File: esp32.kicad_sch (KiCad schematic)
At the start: 50 parts, among them J4 TC2030-IDC, J5 Conn_01x04, J6 Conn_01x06, J8 USB_C_Receptacle_USB2.0, SW1 SWITCH-SPST, SW2 SWITCH-SPST, U5 SN74AVC4T774, U6 ESP32-S3-WROOM-1, Y1 32.768kHz

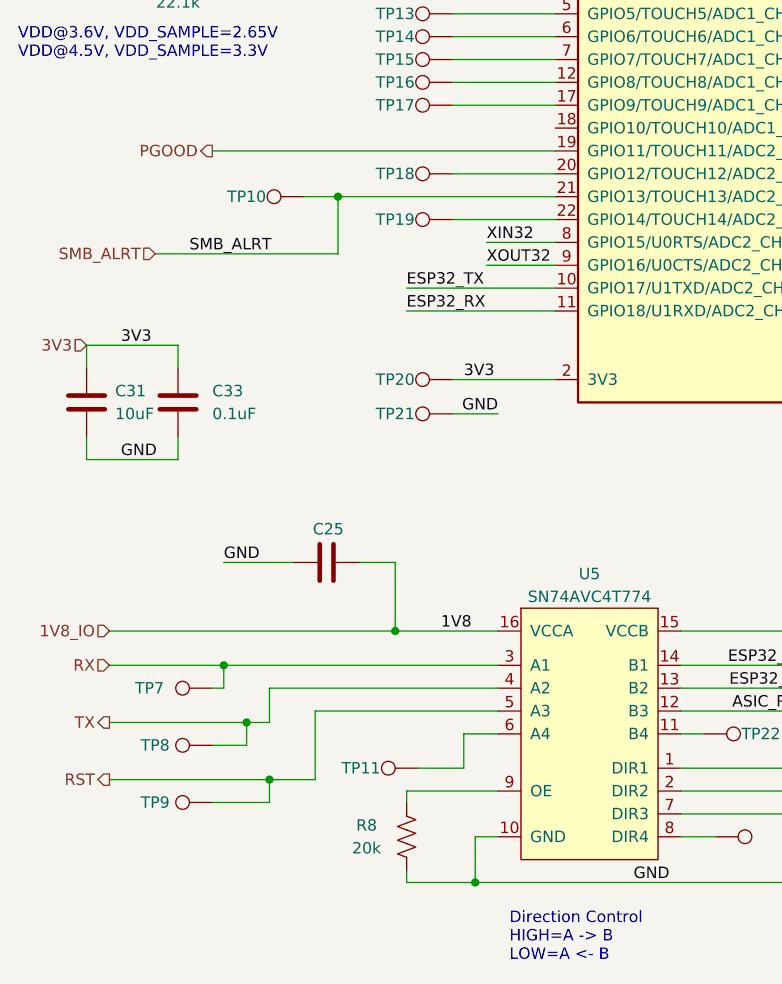
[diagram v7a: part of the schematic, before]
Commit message: add voltage domain sense signals to the ESP32 ADC
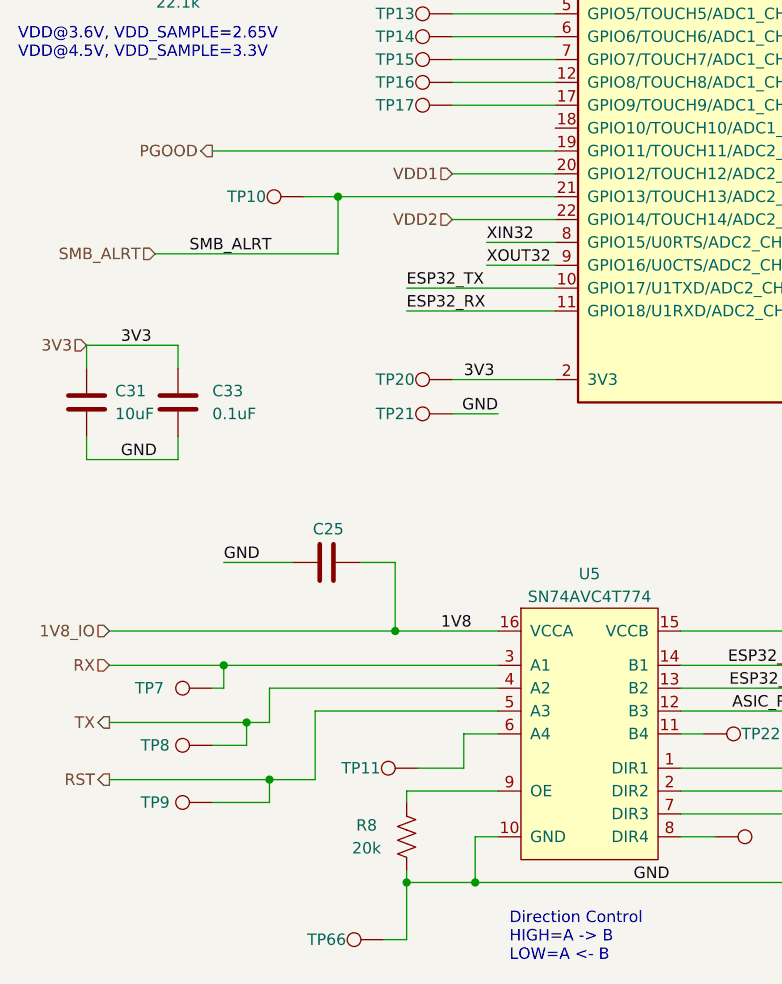
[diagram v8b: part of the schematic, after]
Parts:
- removed TP18, TP19: TestPoint, TestPoint:TestPoint_Pad_D1.0mm, symbol Connector:TestPoint
- added TP66: TestPoint, TestPoint:TestPoint_Pad_D1.0mm, symbol Connector:TestPoint
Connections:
- net GND: now also TP66.1
- net VDD1: now reaches U6.20 (GPIO12/TOUCH12/ADC2_CH1/FSPICLK/FSPIIO6/SUBSPICLK)
- net VDD2: now reaches U6.22 (GPIO14/TOUCH14/ADC2_CH3/FSPIWP/FSPIDQS/SUBSPIWP)
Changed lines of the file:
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@@
 	)
 	(junction
+		(at 57.15 185.42)
+		(diameter 0)
+		(color 0 0 0 0)
+	)
+	(junction
 		(at 36.83 161.29)
 		(diameter 0)
@@
 	(wire
 		(pts
+			(xy 57.15 191.77) (xy 57.15 185.42)
+		)
+		(stroke
+			(width 0)
+			(type default)
+		)
+	)
+	(wire
+		(pts
 			(xy 39.37 49.53) (xy 46.99 49.53)
 		)
@@
 	(wire
 		(pts
+			(xy 54.61 191.77) (xy 57.15 191.77)
+		)
+		(stroke
+			(width 0)
+			(type default)
+		)
+	)
+	(wire
+		(pts
 			(xy 21.59 125.73) (xy 21.59 128.27)
 		)
@@
 		)
 	)
+	(hierarchical_label "VDD2"
+		(shape input)
+		(at 62.23 111.76 180)
+		(fields_autoplaced yes)
+		(effects
+			(font
+				(size 1.27 1.27)
+			)
+			(justify right)
+		)
+	)
 	(hierarchical_label "SCL"
 		(shape input)
@@
 		)
 	)
+	(hierarchical_label "VDD1"
+		(shape input)
+		(at 62.23 106.68 180)
+		(fields_autoplaced yes)
+		(effects
+			(font
+				(size 1.27 1.27)
+			)
+			(justify right)
+		)
+	)
 	(hierarchical_label "SDA"
 		(shape input)
@@
 	(symbol
 		(lib_id "Connector:TestPoint")
+		(at 54.61 191.77 90)
+		(mirror x)
+		(unit 1)
+		(exclude_from_sim no)
+		(in_bom no)
+		(on_board yes)
+		(dnp no)
+		(property "Reference" "TP66"
+			(at 48.26 191.77 90)
+			(effects
+				(font
+					(size 1.27 1.27)
+				)
+			)
+		)
+		(property "Value" "TestPoint"
+			(at 48.895 193.0399 90)
+			(effects
+				(font
+					(size 1.27 1.27)
+				)
+				(justify left)
+				(hide yes)
+			)
+		)
+		(property "Footprint" "TestPoint:TestPoint_Pad_D1.0mm"
+			(at 54.61 196.85 0)
+			(effects
+				(font
+					(size 1.27 1.27)
+				)
+				(hide yes)
+			)
+		)
+		(property "Datasheet" "~"
+			(at 54.61 196.85 0)
+			(effects
+				(font
+					(size 1.27 1.27)
+				)
+				(hide yes)
+			)
+		)
+		(property "Description" ""
+			(at 54.61 191.77 0)
+			(effects
+				(font
+					(size 1.27 1.27)
+				)
+				(hide yes)
+			)
+		)
+		(pin "1"
+		)
+		(instances
+			(project "bitaxeHex"
+				(path "/e63e39d7-6ac0-4ffd-8aa3-1841a4541b55/ca857324-2ec8-447e-bd58-90d0c2e6b6d7"
+					(reference "TP66")
+					(unit 1)
+				)
+			)
+		)
+	)
+	(symbol
+		(lib_id "Connector:TestPoint")
 		(at 91.44 180.34 270)
 		(mirror x)
@@
 	)
 	(symbol
-		(lib_id "Connector:TestPoint")
-		(at 62.23 106.68 90)
-		(mirror x)
-		(unit 1)
-		(exclude_from_sim no)
-		(in_bom no)
-		(on_board yes)
-		(dnp no)
-		(property "Reference" "TP18"
-			(at 55.88 106.68 90)
-			(effects
-				(font
-					(size 1.27 1.27)
-				)
-			)
-		)
-		(property "Value" "TestPoint"
-			(at 56.515 107.9499 90)
-			(effects
-				(font
-					(size 1.27 1.27)
-				)
-				(justify left)
-				(hide yes)
-			)
-		)
-		(property "Footprint" "TestPoint:TestPoint_Pad_D1.0mm"
-			(at 62.23 111.76 0)
-			(effects
-				(font
-					(size 1.27 1.27)
-				)
-				(hide yes)
-			)
-		)
-		(property "Datasheet" "~"
-			(at 62.23 111.76 0)
-			(effects
-				(font
-					(size 1.27 1.27)
-				)
-				(hide yes)
-			)
-		)
-		(property "Description" ""
-			(at 62.23 106.68 0)
-			(effects
-				(font
-					(size 1.27 1.27)
-				)
-				(hide yes)
-			)
-		)
-		(pin "1"
-		)
-		(instances
-			(project "bitaxeHex"
-				(path "/e63e39d7-6ac0-4ffd-8aa3-1841a4541b55/ca857324-2ec8-447e-bd58-90d0c2e6b6d7"
-					(reference "TP18")
-					(unit 1)
-				)
-			)
-		)
-	)
-	(symbol
 		(lib_id "bitaxe:SN74AVC4T774")
 		(at 77.47 166.37 0)
@@
 					(unit 1)
 				)
-			)
-		)
-	)
-	(symbol
-		(lib_id "Connector:TestPoint")
-		(at 62.23 111.76 90)
-		(mirror x)
-		(unit 1)
-		(exclude_from_sim no)
-		(in_bom no)
-		(on_board yes)
-		(dnp no)
-		(property "Reference" "TP19"
-			(at 55.88 111.76 90)
-			(effects
-				(font
-					(size 1.27 1.27)
-				)
-			)
-		)
-		(property "Value" "TestPoint"
-			(at 56.515 113.0299 90)
-			(effects
-				(font
-					(size 1.27 1.27)
-				)
-				(justify left)
-				(hide yes)
-			)
-		)
-		(property "Footprint" "TestPoint:TestPoint_Pad_D1.0mm"
-			(at 62.23 116.84 0)
-			(effects
-				(font
-					(size 1.27 1.27)
-				)
-				(hide yes)
-			)
-		)
-		(property "Datasheet" "~"
-			(at 62.23 116.84 0)
-			(effects
-				(font
-					(size 1.27 1.27)
-				)
-				(hide yes)
-			)
-		)
-		(property "Description" ""
-			(at 62.23 111.76 0)
-			(effects
-				(font
-					(size 1.27 1.27)
-				)
-				(hide yes)
-			)
-		)
-		(pin "1"
-		)
-		(instances
-			(project "bitaxeHex"
-				(path "/e63e39d7-6ac0-4ffd-8aa3-1841a4541b55/ca857324-2ec8-447e-bd58-90d0c2e6b6d7"
-					(reference "TP19")
-					(unit 1)
-				)
